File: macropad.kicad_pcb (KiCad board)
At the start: 2 copper layers, 73.3 x 70.1 mm, 8 parts, among them SW1 SW_Push, SW2 SW_Push, SW3 SW_Push, SW5 SW_Push, U1 MOUDLE-SEEEDUINO-XIAO, U3 ER_OLEDM0.91_1x-I2C

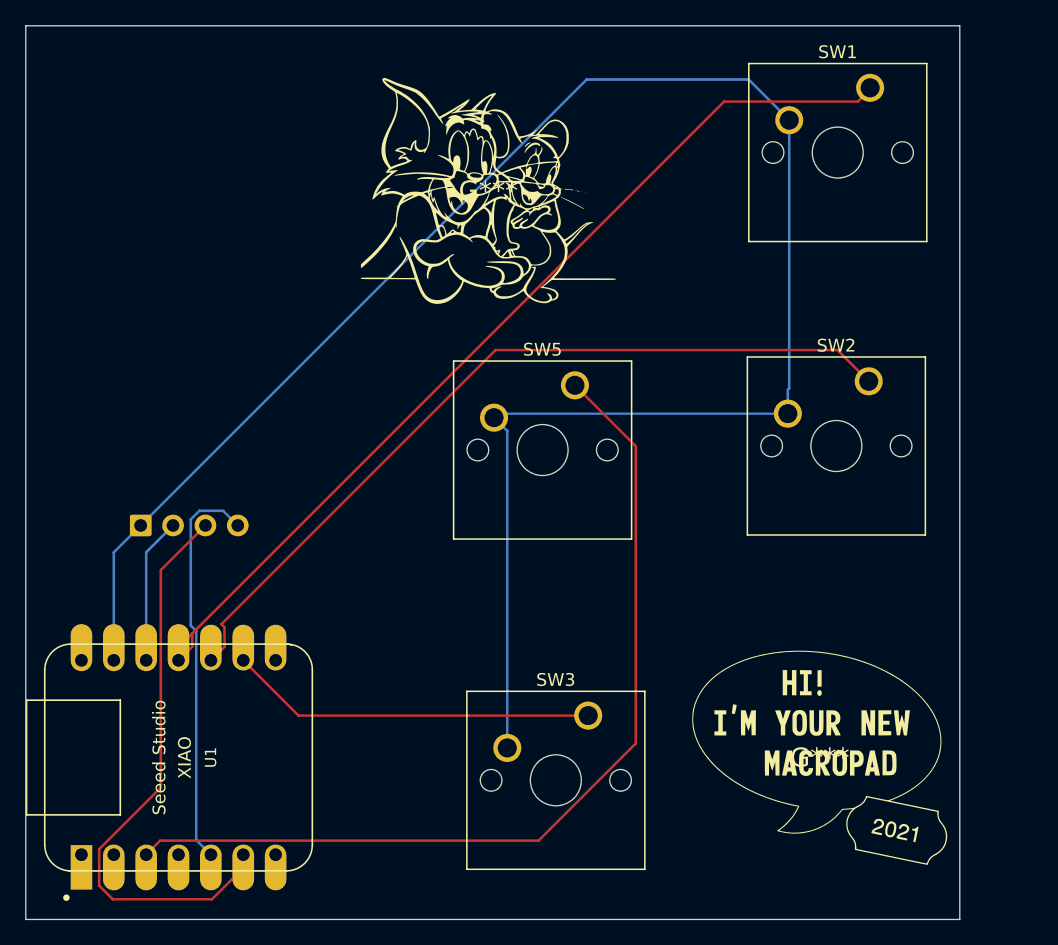
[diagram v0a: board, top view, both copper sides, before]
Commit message: creating the top started
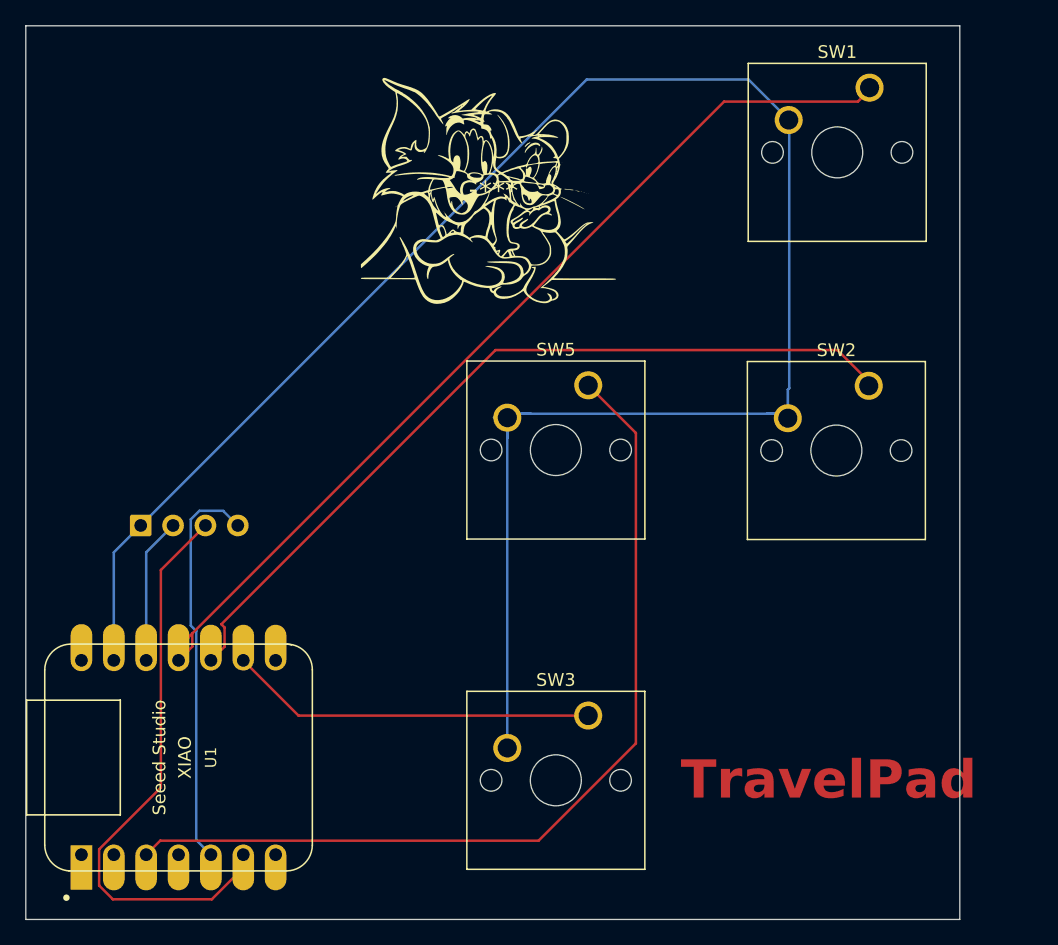
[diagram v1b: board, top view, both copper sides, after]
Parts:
- removed the G*** at (250.5, 101.7)
- moved SW5 1.04 mm to (232.3, 72.5)
- moved SW2 0.36 mm to (254.4, 72.5)
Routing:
- net GND: track 150.8 -> 156.4 mm
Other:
- board text added: "TravelPad"
